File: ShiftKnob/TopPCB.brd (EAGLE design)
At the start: 33 x 33 mm, 9 parts

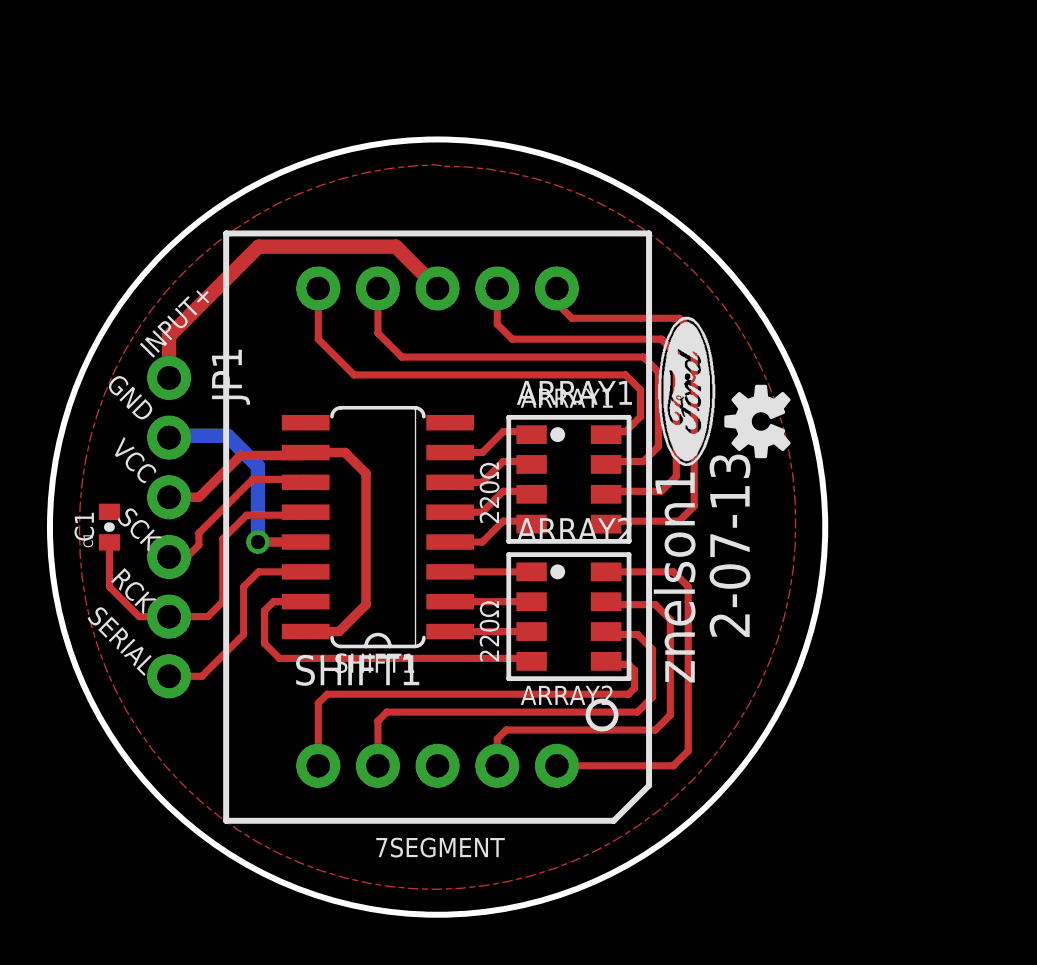
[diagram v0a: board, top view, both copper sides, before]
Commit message: move C1, add (2) 0.1in holes for assembly and rework silk screens. move PCB to be centered at .85x.85 like bottomPCB
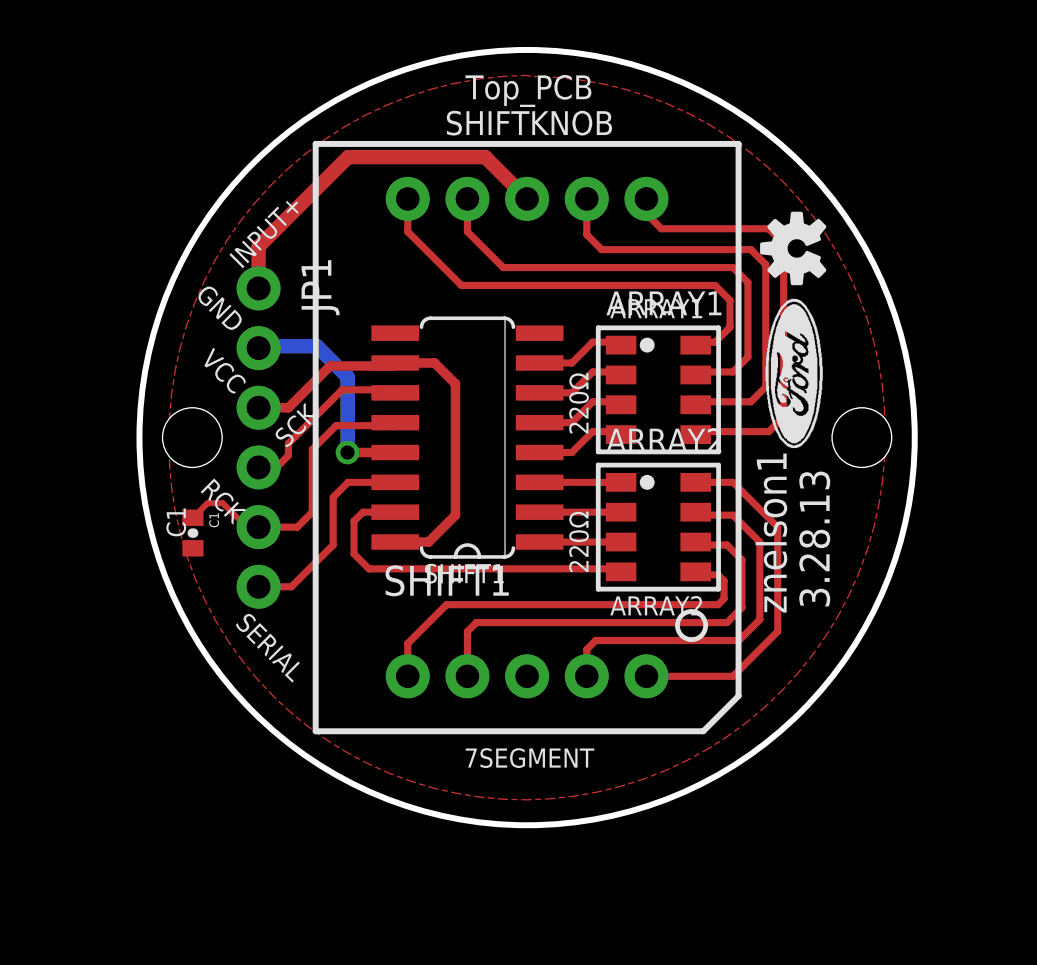
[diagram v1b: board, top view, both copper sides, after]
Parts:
- moved U$1 7.52 mm to (33.1, 29.6)
- moved ARRAY1 5.39 mm to (27.2, 23.6)
- moved ARRAY2 5.39 mm to (27.2, 17.8)
- moved JP1 5.39 mm to (10.2, 27.9)
- moved SHIFT1 5.39 mm to (19.1, 21.6)
- moved 7SEGMENT 5.39 mm to (21.6, 21.6)
- moved C1 3.57 mm to (7.37, 17.5), turned to 270 degrees
- moved U$2 3.31 mm to (23.9, 25.7)
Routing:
- net N$1: track 16.6 -> 15.1 mm
- net RCK: track 14.2 -> 12.7 mm
- net N$3: track 18.5 -> 17.8 mm
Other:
- board text added: "3.28.13"
- board text added: "Top_PCB SHIFTKNOB"
- board text removed: "2-07-13"

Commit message: use (2) 4 pin connectors rather than a 6 pin connector. Board layout and schematic preliminarily complete.
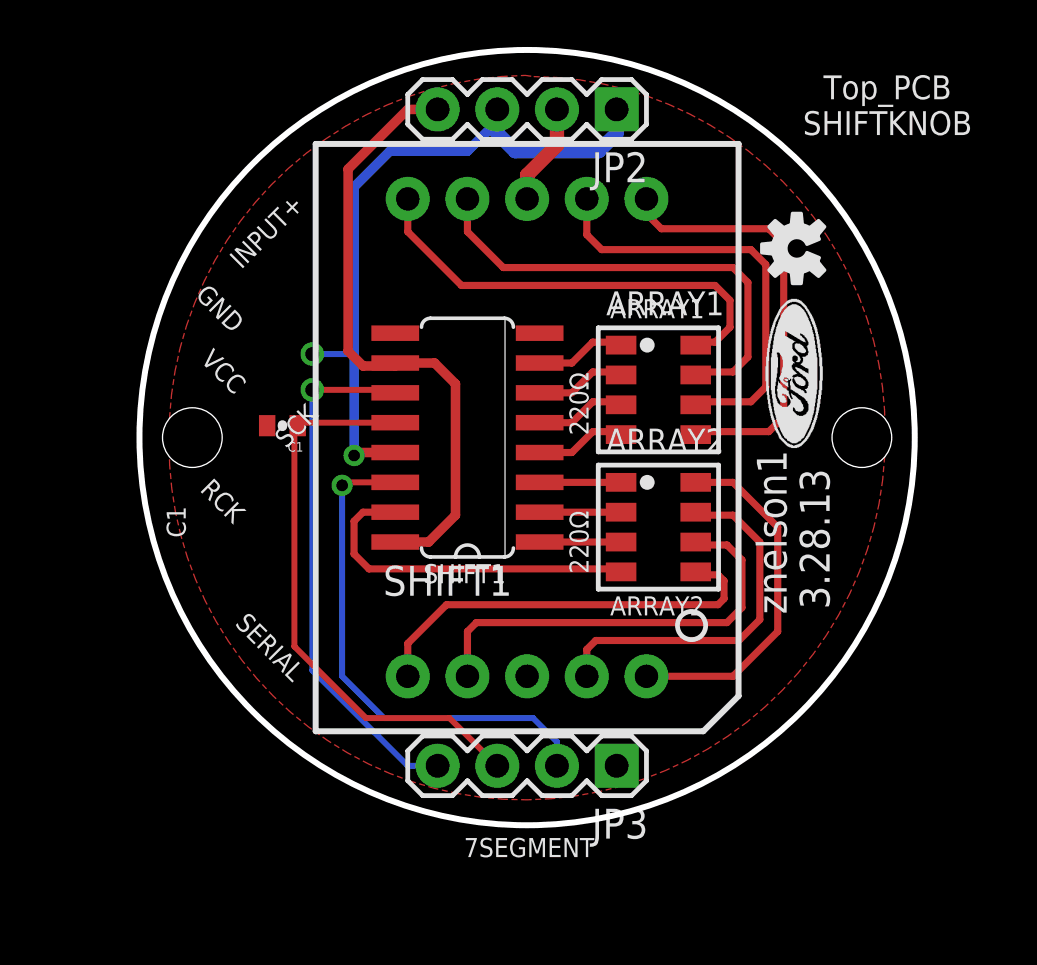
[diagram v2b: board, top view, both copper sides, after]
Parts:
- removed JP1: 6 PIN 90degree Header, SparkFun-Connectors:1X06
- added JP2, JP3: (no value), SparkFun-Connectors:1X04
- moved C1 5.95 mm to (11.2, 22.1), turned to 180 degrees
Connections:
- net GND: now also JP2.1, JP2.3, JP3.1; no longer JP1.2
- net INPUT+: now also JP2.2; no longer JP1.1
- net RCK: now also JP3.3; no longer JP1.5
- net SCK: now also JP3.4; no longer JP1.4
- net SERIAL: now also JP3.2; no longer JP1.6
- net VCC: now also JP2.4; no longer JP1.3
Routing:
- net GND: track 9.61 -> 30.2 mm, vias 1 -> 2
- net SCK: track 7.53 -> 22.5 mm, vias 0 -> 1
- net SERIAL: track 8.85 -> 21.8 mm, vias 0 -> 1
- net RCK: track 12.7 -> 24.4 mm
- net INPUT+: track 15.5 -> 4.34 mm
- net VCC: track 18.2 -> 26.6 mm
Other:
- board text added: "02"
- board text removed: "01"

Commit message: redo silk screen pin labels. DRC checks out OK.
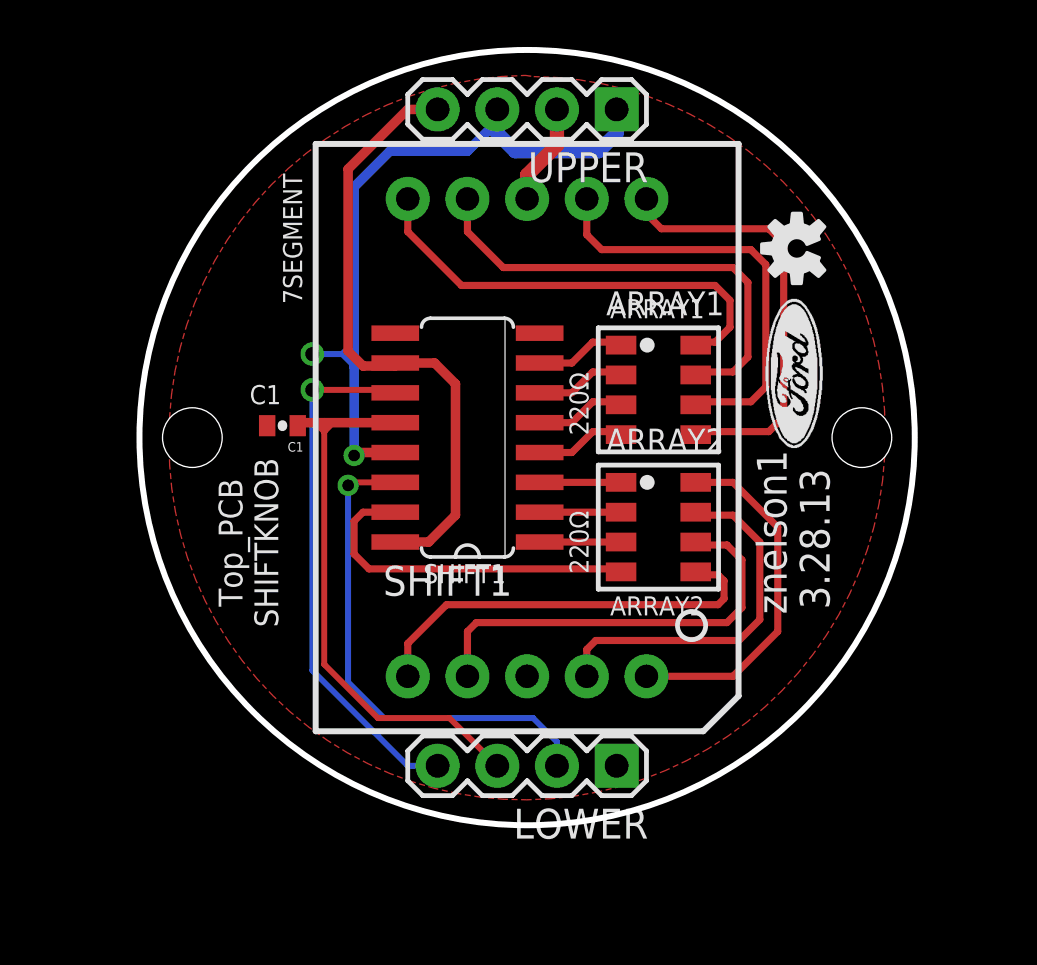
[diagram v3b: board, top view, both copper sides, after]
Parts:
- renumbered JP2 to UPPER, JP3 to LOWER
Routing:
- net GND: track 30.2 -> 31.7 mm
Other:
- board text added: "IN+"
- board text added: "SER"
- board text removed: "INPUT+"
- board text removed: "SERIAL"
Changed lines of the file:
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@@
 <rectangle x1="31.0515" y1="24.2951" x2="32.4993" y2="24.3205" layer="21" rot="R90"/>
 <rectangle x1="31.4325" y1="24.2951" x2="32.0675" y2="24.3205" layer="21" rot="R90"/>
-<text x="9.4234" y="28.7274" size="0.8128" layer="21" font="vector" rot="R45">INPUT+</text>
-<text x="9.6266" y="26.5684" size="0.8128" layer="21" font="vector" rot="R135">GND</text>
-<text x="9.7028" y="23.9522" size="0.8128" layer="21" font="vector" rot="R135">VCC</text>
-<text x="12.1666" y="23.0886" size="0.8128" layer="21" font="vector" rot="R225">SCK</text>
-<text x="9.652" y="18.4658" size="0.8128" layer="21" font="vector" rot="R135">RCK</text>
-<text x="9.1186" y="13.6398" size="0.8128" layer="21" font="vector" rot="R315">SERIAL</text>
+<text x="21.59" y="34.036" size="0.8128" layer="22" font="vector" rot="MR180">IN+</text>
+<text x="24.384" y="34.036" size="0.8128" layer="22" font="vector" rot="MR180">GND</text>
+<text x="16.51" y="34.036" size="0.8128" layer="22" font="vector" rot="MR180">VCC</text>
+<text x="16.51" y="9.906" size="0.8128" layer="22" font="vector" rot="MR180">SCK</text>
+<text x="19.05" y="9.906" size="0.8128" layer="22" font="vector" rot="MR180">RCK</text>
+<text x="21.59" y="9.906" size="0.8128" layer="22" font="vector" rot="MR180">SER</text>
 <text x="25.1206" y="14.0208" size="0.8128" layer="21" font="vector">ARRAY2</text>
 <text x="24.2062" y="15.7988" size="0.8128" layer="21" font="vector" rot="R90">220Ω</text>
@@
 <text x="25.1206" y="26.67" size="0.8128" layer="21" font="vector">ARRAY1</text>
 <text x="17.1704" y="15.3924" size="0.8128" layer="21" font="vector">SHIFT1</text>
-<text x="6.2484" y="18.669" size="0.8128" layer="21" font="vector" rot="R270">C1</text>
+<text x="9.779" y="23.0124" size="0.8128" layer="21" font="vector">C1</text>
 <text x="21.7932" y="28.194" size="1.778" layer="22" rot="MR270">znelson1</text>
 <text x="18.6182" y="26.4414" size="1.778" layer="22" rot="MR270">3.28.13</text>
@@
 <rectangle x1="24.3713" y1="20.1803" x2="25.8191" y2="20.2057" layer="22" rot="R90"/>
 <rectangle x1="24.8031" y1="20.1803" x2="25.4381" y2="20.2057" layer="22" rot="R90"/>
-<text x="18.8976" y="3.7338" size="0.8128" layer="21" font="vector">7SEGMENT</text>
+<text x="12.0142" y="27.2796" size="0.8128" layer="21" font="vector" rot="R90">7SEGMENT</text>
 <text x="15.24" y="-40.64" size="3.81" layer="48">Zachary Nelson
 znelson1@ford.com</text>
@@
 <hole x="7.3406" y="21.59" drill="2.54"/>
 <hole x="35.8394" y="21.59" drill="2.54"/>
-<text x="36.9316" y="35.7378" size="1.016" layer="21" font="vector" align="center">Top_PCB
+<text x="9.7282" y="17.1196" size="1.016" layer="21" font="vector" rot="R90" align="center">Top_PCB
 SHIFTKNOB</text>
+<text x="24.13" y="9.906" size="0.8128" layer="22" font="vector" rot="MR180">GND</text>
+<text x="19.05" y="34.036" size="0.8128" layer="22" font="vector" rot="MR180">GND</text>
 </plain>
 <attributes>
@@
 <element name="U$1" library="SparkFun" package="OSHW-LOGO-S" value="OSHW-LOGOS" x="33.0708" y="29.6418" rot="R90"/>
 <element name="U$3" library="FORD_frames" package="DOCFIELD" value="" x="-49.53" y="-48.26"/>
-<element name="JP2" library="SparkFun-Connectors" package="1X04" value="" x="25.4" y="35.56" rot="R180"/>
-<element name="JP3" library="SparkFun-Connectors" package="1X04" value="" x="25.4" y="7.62" rot="R180"/>
+<element name="UPPER" library="SparkFun-Connectors" package="1X04" value="" x="25.4" y="35.56" rot="R180"/>
+<element name="LOWER" library="SparkFun-Connectors" package="1X04" value="" x="25.4" y="7.62" rot="R180"/>
 </elements>
 <signals>
@@
 <vertex x="21.59" y="6.1722" curve="-90.979389"/>
 </polygon>
-<contactref element="JP2" pad="3"/>
-<contactref element="JP2" pad="1"/>
-<contactref element="JP3" pad="1"/>
+<contactref element="UPPER" pad="3"/>
+<contactref element="UPPER" pad="1"/>
+<contactref element="LOWER" pad="1"/>
 <wire x1="20.32" y1="35.56" x2="20.32" y2="35.052" width="0.6096" layer="16"/>
 <wire x1="20.32" y1="35.052" x2="20.32" y2="34.544" width="0.6096" layer="16"/>
@@
 <wire x1="14.224" y1="20.955" x2="14.224" y2="20.828" width="0.4064" layer="1"/>
 <via x="14.224" y="20.828" extent="1-16" drill="0.5"/>
-<wire x1="14.224" y1="20.828" x2="14.224" y2="25.146" width="0.4064" layer="16"/>
-<wire x1="14.224" y1="25.146" x2="14.224" y2="32.258" width="0.4064" layer="16"/>
+<wire x1="14.224" y1="20.828" x2="14.224" y2="24.638" width="0.4064" layer="16"/>
+<wire x1="14.224" y1="24.638" x2="14.224" y2="25.146" width="0.4064" layer="16"/>
+<wire x1="14.224" y1="25.146" x2="14.224" y2="25.654" width="0.4064" layer="16"/>
+<wire x1="14.224" y1="25.654" x2="14.224" y2="32.258" width="0.4064" layer="16"/>
 <wire x1="14.224" y1="32.258" x2="15.748" y2="33.782" width="0.4064" layer="16"/>
 <wire x1="15.748" y1="33.782" x2="19.05" y2="33.782" width="0.4064" layer="16"/>
@@
 <wire x1="14.112" y1="20.716" x2="14.224" y2="20.828" width="0.4064" layer="1"/>
 <via x="12.446" y="25.146" extent="1-16" drill="0.6"/>
-<wire x1="12.446" y1="25.146" x2="14.224" y2="25.146" width="0.254" layer="16"/>
+<wire x1="12.446" y1="25.146" x2="13.716" y2="25.146" width="0.254" layer="16"/>
+<wire x1="13.716" y1="25.146" x2="14.224" y2="25.146" width="0.254" layer="16"/>
+<wire x1="13.716" y1="25.146" x2="14.224" y2="24.638" width="0.254" layer="16"/>
+<wire x1="13.716" y1="25.146" x2="14.224" y2="25.654" width="0.254" layer="16"/>
 </signal>
 <signal name="VCC">
@@
 <wire x1="18.542" y1="23.876" x2="17.653" y2="24.765" width="0.4064" layer="1"/>
 <wire x1="17.653" y1="24.765" x2="15.9766" y2="24.765" width="0.4064" layer="1"/>
-<contactref element="JP2" pad="4"/>
+<contactref element="UPPER" pad="4"/>
 <wire x1="17.78" y1="35.56" x2="16.51" y2="35.56" width="0.4064" layer="1"/>
 <wire x1="16.51" y1="35.56" x2="13.97" y2="33.02" width="0.4064" layer="1"/>
@@
 <signal name="INPUT+">
 <contactref element="7SEGMENT" pad="8"/>
-<contactref element="JP2" pad="2"/>
+<contactref element="UPPER" pad="2"/>
 <wire x1="21.59" y1="31.75" x2="21.59" y2="32.766" width="0.6096" layer="1"/>
 <wire x1="21.59" y1="32.766" x2="22.86" y2="34.036" width="0.6096" layer="1"/>
@@
 <signal name="SCK">
 <contactref element="SHIFT1" pad="11"/>
-<contactref element="JP3" pad="4"/>
+<contactref element="LOWER" pad="4"/>
 <wire x1="17.78" y1="7.62" x2="16.51" y2="7.62" width="0.254" layer="16"/>
 <wire x1="16.51" y1="7.62" x2="12.446" y2="11.684" width="0.254" layer="16"/>
@@
 <signal name="SERIAL">
 <contactref element="SHIFT1" pad="14"/>
-<contactref element="JP3" pad="2"/>
+<contactref element="LOWER" pad="2"/>
 <wire x1="22.86" y1="7.62" x2="22.86" y2="8.636" width="0.254" layer="16"/>
 <wire x1="22.86" y1="8.636" x2="21.844" y2="9.652" width="0.254" layer="16"/>
 <wire x1="21.844" y1="9.652" x2="15.494" y2="9.652" width="0.254" layer="16"/>
-<wire x1="15.494" y1="9.652" x2="13.716" y2="11.43" width="0.254" layer="16"/>
-<wire x1="13.716" y1="11.43" x2="13.716" y2="19.558" width="0.254" layer="16"/>
-<via x="13.716" y="19.558" extent="1-16" drill="0.5"/>
-<wire x1="13.716" y1="19.558" x2="13.843" y2="19.685" width="0.254" layer="1"/>
-<wire x1="13.843" y1="19.685" x2="15.9766" y2="19.685" width="0.254" layer="1"/>
+<wire x1="15.494" y1="9.652" x2="13.97" y2="11.176" width="0.254" layer="16"/>
+<wire x1="13.97" y1="11.176" x2="13.97" y2="19.558" width="0.254" layer="16"/>
+<via x="13.97" y="19.558" extent="1-16" drill="0.5"/>
+<wire x1="13.97" y1="19.558" x2="14.097" y2="19.685" width="0.254" layer="1"/>
+<wire x1="14.097" y1="19.685" x2="15.9766" y2="19.685" width="0.254" layer="1"/>
 </signal>
 <signal name="N$1">
@@
 <contactref element="SHIFT1" pad="12"/>
 <contactref element="C1" pad="1"/>
-<contactref element="JP3" pad="3"/>
-<wire x1="15.9766" y1="22.225" x2="11.953" y2="22.225" width="0.254" layer="1"/>
+<contactref element="LOWER" pad="3"/>
 <wire x1="11.953" y1="22.225" x2="11.826" y2="22.098" width="0.254" layer="1"/>
 <wire x1="20.32" y1="7.62" x2="18.288" y2="9.652" width="0.254" layer="1"/>
-<wire x1="18.288" y1="9.652" x2="14.732" y2="9.652" width="0.254" layer="1"/>
-<wire x1="14.732" y1="9.652" x2="11.684" y2="12.7" width="0.254" layer="1"/>
-<wire x1="11.684" y1="12.7" x2="11.684" y2="21.956" width="0.254" layer="1"/>
+<wire x1="18.288" y1="9.652" x2="15.24" y2="9.652" width="0.254" layer="1"/>
+<wire x1="15.24" y1="9.652" x2="12.954" y2="11.938" width="0.254" layer="1"/>
+<wire x1="12.954" y1="11.938" x2="12.954" y2="21.844" width="0.254" layer="1"/>
+<wire x1="12.954" y1="21.844" x2="12.954" y2="22.225" width="0.254" layer="1"/>
 <wire x1="11.684" y1="21.956" x2="11.826" y2="22.098" width="0.254" layer="1"/>
+<wire x1="15.9766" y1="22.225" x2="12.954" y2="22.225" width="0.4064" layer="1"/>
+<wire x1="12.954" y1="22.225" x2="11.826" y2="22.225" width="0.4064" layer="1"/>
+<wire x1="11.826" y1="22.225" x2="11.826" y2="22.098" width="0.4064" layer="1"/>
+<wire x1="12.954" y1="21.844" x2="13.208" y2="22.098" width="0.254" layer="1"/>
+<wire x1="12.954" y1="21.844" x2="12.7" y2="22.098" width="0.254" layer="1"/>
 </signal>
 <signal name="N$17">
